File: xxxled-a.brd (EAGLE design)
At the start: 100 x 80 mm, 9 parts, among them J2 BAT+, J3 LED-, J4 BAT+, J5 LED-, Q1 TIP120

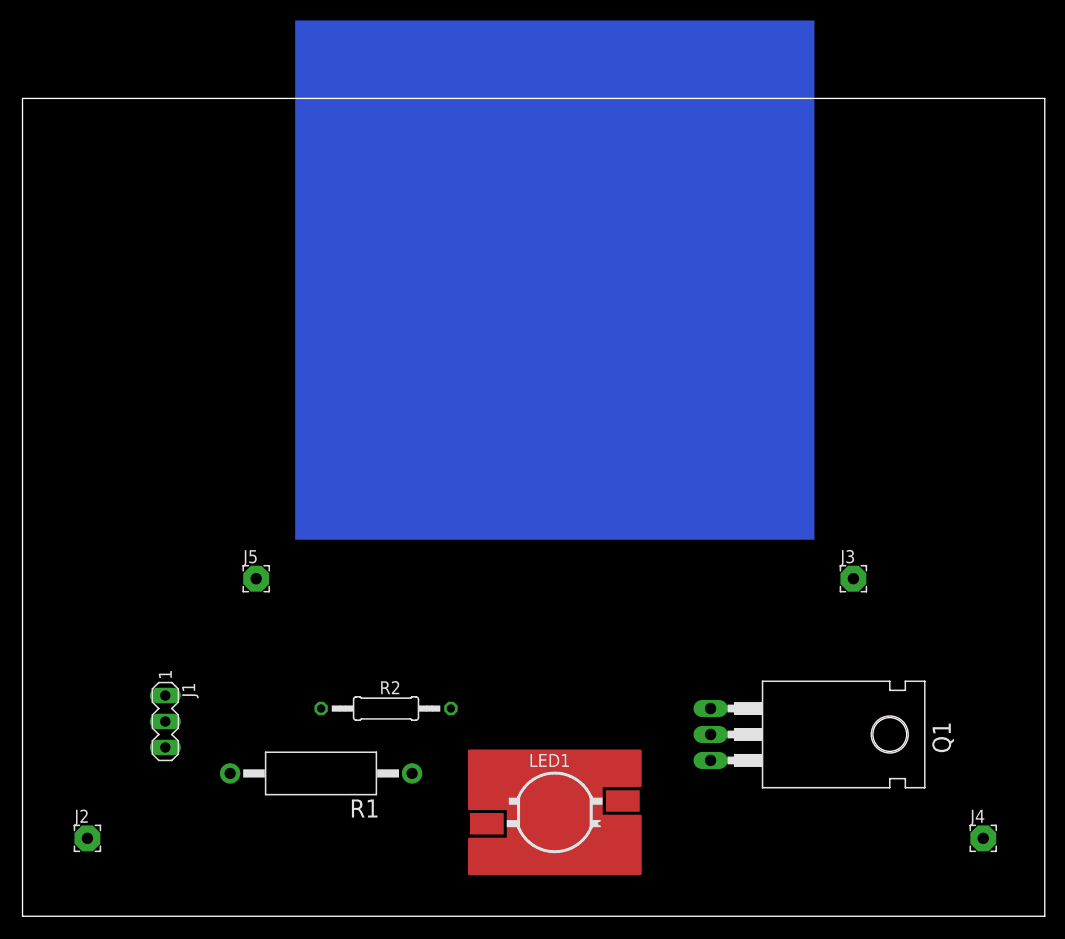
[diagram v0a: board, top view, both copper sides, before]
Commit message: First draft single-sided PCB layout
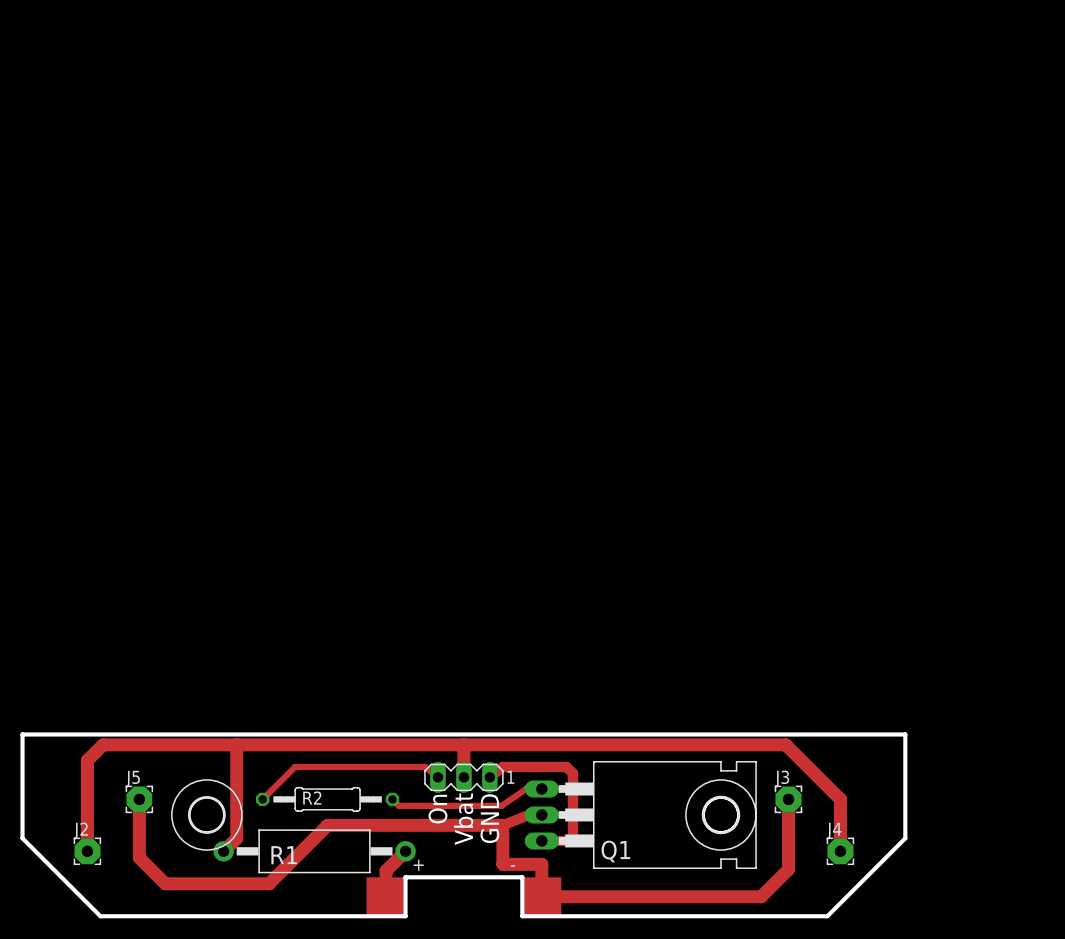
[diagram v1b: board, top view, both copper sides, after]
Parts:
- added U$1, U$2: (no value), holes:3,3
- LED1: device xxxled:Z-POWER-LED-DOME-TYPE -> xxxled:POWER_LED_EDGE
- moved J1 29.7 mm to (43.2, 13.6), turned to 180 degrees
- moved J5 24.4 mm to (11.4, 11.4)
- moved J3 22.5 mm to (74.9, 11.4)
- moved Q1 18.3 mm to (57.1, 9.91)
- moved J4 14.0 mm to (80.0, 6.35)
- moved LED1 10.9 mm to (43.2, 3.81)
- moved R2 10.6 mm to (29.8, 11.4)
- moved R1 7.65 mm to (28.6, 6.35)
- moved J2 1.27 mm to (6.35, 6.35)
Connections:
- net N$1: now also J1.3; no longer J1.2
- net N$3: now also LED1.P$C; no longer LED1.C
- net N$4: now also LED1.P$A; no longer LED1.A
- net N$5: now also J1.2; no longer J1.3
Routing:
- net N$5: track 0.00 -> 104.6 mm
- net N$3: track 0.00 -> 91.6 mm
- net N$1: track 0.00 -> 18.8 mm
- net N$7: track 0.00 -> 18.1 mm
- net N$2: track 0.00 -> 15.4 mm
- net N$4: track 0.00 -> 5.24 mm
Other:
- board size 100 x 80 mm -> 86.4 x 17.8 mm
- board text added: "GND"
- board text added: "On"
- board text added: "Vbat"

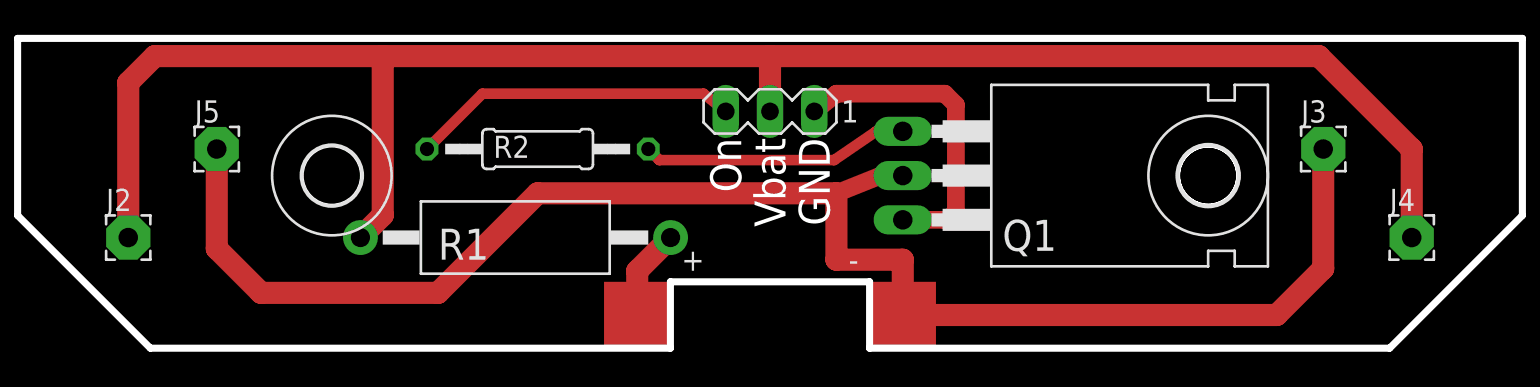
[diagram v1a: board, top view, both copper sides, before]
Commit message: * added J2 to connect the two board clusters on one stake to each other * Tidied silkscreen layout * Moved mounting holes (and Q1) in a bit * Layout with all 50mil traces * Down to 1/2W for R1, still plenty and this saves money and space
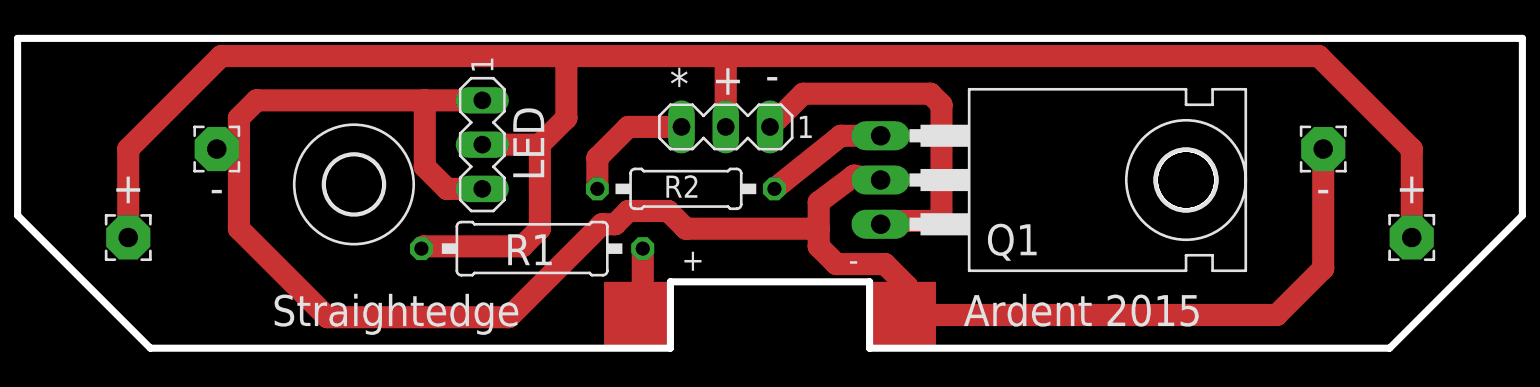
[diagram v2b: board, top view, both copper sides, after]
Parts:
- added J6: LED-, wirepad:2,54/1,1
- J2: value BAT+ -> (none); device wirepad:2,54/1,1 -> con-lstb:MA03-1
- J3, J5: value LED- -> BAT+
- J4: value BAT+ -> LED-
- R1: value 4 ohm, 1W -> 4.7 1/2W; device resistor-power:AC01 -> resistor:0309/12
- R2: value 470 -> 470 1/4W; device resistor:0207/12 -> resistor:0207/10
- moved J3 68.8 mm to (6.35, 6.35)
- moved J5 68.8 mm to (80.0, 6.35)
- moved J2 21.0 mm to (26.7, 11.7), turned to 270 degrees
- moved R2 8.81 mm to (38.4, 9.14)
- moved J4 7.18 mm to (74.9, 11.4)
- moved J1 2.69 mm to (40.6, 12.7)
- moved U$2 1.37 mm to (19.3, 9.40)
- moved Q1 1.30 mm to (55.9, 9.65)
- moved U$1 1.30 mm to (67.1, 9.65)
- moved R1 1.14 mm to (29.5, 5.71)
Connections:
- net N$3: now also J2.1, J2.3, J4.1, J6.1; no longer J3.1, J5.1
- net N$5: now also J2.2, J3.1, J5.1; no longer J2.1, J4.1
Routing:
- net N$3: track 91.6 -> 116.2 mm
- net N$1: track 18.8 -> 7.34 mm
- net N$5: track 104.6 -> 113.4 mm
- net N$2: track 15.4 -> 7.17 mm
- net N$7: track 18.1 -> 21.2 mm
- net N$4: track 5.24 -> 3.86 mm
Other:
- board text added: "*"
- board text added: "+"
- board text added: "-"
- board text added: "Ardent 2015"
- board text added: "LED"
- board text added: "Straightedge"
- board text removed: "GND"
- board text removed: "On"
- board text removed: "Vbat"

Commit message: Switch to 2.7 ohm power resistor
With the prototype PCB and 4 LEDs, this gives a peak current of ~0.75 A at 4.5V
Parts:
- R1: value 4.7 1/2W -> 2.7 1/2W
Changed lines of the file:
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@@
 <attribute name="NAME" x="55.5625" y="5.334" size="1.778" layer="25" ratio="10"/>
 </element>
-<element name="R1" library="resistor" package="0309/12" value="4.7 1/2W" x="29.5275" y="5.715" smashed="yes" rot="R180">
+<element name="R1" library="resistor" package="0309/12" value="2.7 1/2W" x="29.5275" y="5.715" smashed="yes" rot="R180">
 <attribute name="NAME" x="27.94" y="4.7625" size="1.778" layer="25" ratio="10"/>
 </element>
